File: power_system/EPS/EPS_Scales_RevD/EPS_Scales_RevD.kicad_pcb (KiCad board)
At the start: 4 copper layers, 95.2 x 66 mm, 253 parts, among them J1 Input Power, J10 DF11-16DP-2DSA, J11 DN-T1-GE3_VIS, J12 DF11-16DP-2DSA, J15 DN-T1-GE3_VIS, J16 Conn_01x04, J18 Conn_01x04, J2 Conn_01x01_Socket, J3 Conn_01x01_Socket, J4 Conn_01x01_Socket, J5 Conn_01x01_Socket, J6 DF11-16DP-2DSA, J7 DN-T1-GE3_VIS, J8 Conn_01x04, U1 LTC4365, U10 LTC4365, U11 LT8638S, U12 INA230, U13 TLV1704, U14 TLV1704, U2 LT8638SEVPBF, U3 INA230, U4 TLV1704, U5 LTC4365, U6 LT8638S, U7 LTC6902, U8 INA230, U9 TCA4307DGKR

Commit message: Lots of Goodies
Updated Con. Ops
Updated Footprint Assignments for R and C, WIP
Fixed Incorrect Resistor Values
Updated footprints for LEDs
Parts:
- removed C1, C14, C15, C17, C18, C19, C2, C20, C21, C22, C25, C3, C34, C35, C45, C5, C53, C54, C56, C57, C58, C59, C60, C61, C62, C63, C64, C65, C66, C67: 10u, Capacitor_SMD:C_1210_3225Metric
- removed C10, C29, C30, C37, C49: 0.1u, Capacitor_SMD:C_1210_3225Metric
- removed C12, C13, C32, C33, C51, C52: 47u, Capacitor_SMD:C_1210_3225Metric
- removed C16, C28, C36, C47, C55, C8: 1u, Capacitor_SMD:C_1210_3225Metric
- removed C23, C4, C43: 22u, Capacitor_SMD:C_1210_3225Metric
- removed C24, C44, C6: 1u, Capacitor_SMD:C_0603_1608Metric
- removed C26: 10n, Capacitor_SMD:C_0603_1608Metric
- removed C27, C9: 220p, Capacitor_SMD:C_0603_1608Metric
- removed C31, C38, C39: 22p, easyeda2kicad:C1206
- removed C46: 20n, Capacitor_SMD:C_0603_1608Metric
- removed C48: 1n, Capacitor_SMD:C_0603_1608Metric
- removed C7: 100n, Capacitor_SMD:C_0603_1608Metric
- removed D1, D10, D12, D3, D7, D9: 1N4151WS, RevC Footprints:SODFL2512X100N
- removed D11, D2, D8: GREEN, LED_SMD:LED_0603_1608Metric
- removed G*** (x3): LOGO, LOGO
- removed J1: Input Power, Connector_AMASS:AMASS_XT60PW-F_1x02_P7.20mm_Horizontal
- removed J10, J12, J6: DF11-16DP-2DSA, RevC Footprints:DF1116DP2DSA08
- removed J11, J15, J7: DN-T1-GE3_VIS, RevC Footprints:SISB46DN-T1-GE3
- removed J16, J18, J8: Conn_01x04, Connector_PinSocket_2.54mm:PinSocket_1x04_P2.54mm_Vertical
- removed J2, J3, J4, J5: Conn_01x01_Socket, MountingHole:MountingHole_2.5mm_Pad
- removed JP1, JP4, JP5: SolderJumper_2_Open, Jumper:SolderJumper-2_P1.3mm_Open_RoundedPad1.0x1.5mm
- removed L3: 10u, easyeda2kicad:IND-SMD_L13.8-W12.6_MHCC12050
- removed L4: 2.2u, RevC Footprints:XEL6030
- removed L5: 3.3u, RevC Footprints:XEL6030
- removed OV_TP1, OV_TP2, OV_TP3, TP1, TP10, TP11, TP12, TP13, TP14, TP15, TP16, TP17, TP18, TP19, TP2, TP20, TP28, TP29, TP3, TP30, TP31, TP32, TP33, TP34, TP35, TP36, TP37, TP38, TP39, TP4, TP40, TP41, TP42, TP43, TP44, TP45, TP46, TP47, TP48, TP49, TP5, TP50, TP51, TP52, TP53, TP6, TP7, TP8, TP9, UV_TP1, UV_TP2, UV_TP3: TestPoint, TestPoint:TestPoint_Pad_1.0x1.0mm
- removed R1, R28, R57: 12.9M, Resistor_SMD:R_0603_1608Metric
- removed R10, R38, R66: 10m, Resistor_SMD:R_2512_6332Metric
- removed R100, R101, R21, R23, R24, R25, R27, R31, R39, R5, R61, R77, R79, R8, R80, R81, R83, R94, R96, R97, R98: 100k, Resistor_SMD:R_0603_1608Metric
- removed R11, R67, R84: 10 (1206), Resistor_SMD:R_1206_3216Metric
- removed R12, R13, R14, R18, R19, R32, R42, R43, R44, R45, R46, R47, R48, R6, R62, R68, R69, R70, R74, R75, R85, R86, R87, R91, R92: 10k, Resistor_SMD:R_0603_1608Metric
- removed R15, R16, R17, R65, R71, R72, R73, R88, R89, R9, R90: 3.0k, Resistor_SMD:R_0603_1608Metric
- removed R2, R29, R58: 110k, Resistor_SMD:R_0603_1608Metric
- removed R20, R22, R4, R60, R76, R78, R93, R95: 1k, Resistor_SMD:R_0603_1608Metric
- removed R26, R82, R99: 4.7M, Resistor_SMD:R_0603_1608Metric
- removed R3, R30, R59: 190k, Resistor_SMD:R_0603_1608Metric
- removed R33, R63, R7: 105k, Resistor_SMD:R_0603_1608Metric
- removed R34: 14k, Resistor_SMD:R_0603_1608Metric
- removed R35: 17k, Resistor_SMD:R_0603_1608Metric
- removed R36: 25k, Resistor_SMD:R_0603_1608Metric
- removed R37: 5.5k, Resistor_SMD:R_0603_1608Metric
- removed R40: 150k, Resistor_SMD:R_0603_1608Metric
- removed R41: 50k, Resistor_SMD:R_0603_1608Metric
- removed R64: 22k, Resistor_SMD:R_0603_1608Metric
- removed U1, U10, U5: LTC4365, RevC Footprints:LTC4365
- removed U11, U6: LT8638S, RevC Footprints:LT8638SEVPBF
- removed U12, U3, U8: INA230, RevC Footprints:INA230AIRGTT
- removed U13, U14, U4: TLV1704, Package_SO:TSSOP-14_4.4x5mm_P0.65mm
- removed U2: LT8638SEVPBF, RevC Footprints:LT8638SEVPBF
- removed U7: LTC6902, RevC Footprints:LTC6902
- removed U9: TCA4307DGKR, easyeda2kicad:VSSOP-8_L3.0-W3.0-P0.65-LS4.9-BL
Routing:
- net +3.3V_OBC: track 235.8 -> 0.00 mm, vias 14 -> 0
- net GND: track 167.5 -> 0.00 mm, vias 93 -> 0
- net +V_Batt: track 143.8 -> 0.00 mm, vias 6 -> 0
- net SDA: track 120.9 -> 0.00 mm, vias 6 -> 0
- net SCL: track 119.0 -> 0.00 mm, vias 4 -> 0
- net SYNC_PHASE3: track 86.5 -> 0.00 mm, vias 3 -> 0
- net +5V_Perif: track 84.2 -> 0.00 mm, vias 5 -> 0
- net Net-(U2-BIAS): track 70.0 -> 0.00 mm, vias 2 -> 0
- net Net-(U11-BIAS): track 67.7 -> 0.00 mm, vias 8 -> 0
- net SYNC_PHASE1: track 66.8 -> 0.00 mm, vias 3 -> 0
- net ~{OBC_Toggle_Perif}: track 59.0 -> 0.00 mm, vias 1 -> 0
- net Net-(U6-BIAS): track 58.7 -> 0.00 mm
- net ~{WD_TOGGLE_OBC}: track 57.7 -> 0.00 mm, vias 5 -> 0
- net WDT_WDI_OBC: track 56.6 -> 0.00 mm, vias 1 -> 0
- net +20V_Jetson: track 56.0 -> 0.00 mm, vias 4 -> 0
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- removed copper zone on In2.Cu, net +V_Batt
- removed copper zone on In1.Cu, net GND
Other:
- board outline removed
- board text removed: "Designed by Luca Lanzillotta"
- board text removed: "SCALES EPS Viking 1-A"
- board text removed: "this should work..."

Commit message: More Goodies
Updated Inductor footprints with most readily available LCSC counterparts
Updated XT-60 connector
Updated Edge-Cuts board size
Updated Diode Footprints to fix DRC errors
Started Board layout and copper fills for power and ground
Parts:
- added C1: 10u, Capacitor_SMD:C_1210_3225Metric, F.Cu at (236.0, 106.9)
- added C10: 10n, EPS:C0402, F.Cu at (20.0, 50.5)
- added C11: 100n, EPS:C0402, F.Cu at (20.0, 52.6)
- added C13: 100n, EPS:C0402, F.Cu at (20.0, 54.8)
- added C14: 10p, EPS:C0402, F.Cu at (20.0, 56.9)
- added C15: 100n, EPS:C0402, F.Cu at (20.0, 59.1)
- added C16: 100n, EPS:C0402, F.Cu at (20.0, 61.2)
- added C17: 10u, Capacitor_SMD:C_1210_3225Metric, F.Cu at (32.7, 162.4)
- added C18: 10u, Capacitor_SMD:C_1210_3225Metric, F.Cu at (101.3, 147.0)
- added C19: 10u, Capacitor_SMD:C_1210_3225Metric, F.Cu at (101.3, 151.3)
- added C2: 10u, Capacitor_SMD:C_1210_3225Metric, F.Cu at (236.0, 102.7)
- added C20: 10u, Capacitor_SMD:C_1210_3225Metric, F.Cu at (101.3, 155.5)
- added C21: 10u, Capacitor_SMD:C_1210_3225Metric, F.Cu at (101.3, 159.8)
- added C22: 10u, Capacitor_SMD:C_1210_3225Metric, F.Cu at (101.3, 164.0)
- added C23: 22n, EPS:C0402, F.Cu at (79.7, 54.4)
- added C24: 220n, EPS:C0402, F.Cu at (79.7, 56.5)
- added C25: 2.2n, EPS:C0402, F.Cu at (79.7, 58.6)
- added C26: 10p, EPS:C0402, F.Cu at (79.7, 60.8)
- added C27: 100n, EPS:C0402, F.Cu at (79.7, 63.0)
- added C28: 100n, EPS:C0402, F.Cu at (79.7, 65.1)
- added C29: 0.1u, Capacitor_SMD:C_1210_3225Metric, F.Cu at (71.0, 57.7)
- added C3: 10u, Capacitor_SMD:C_1210_3225Metric, F.Cu at (236.0, 98.4)
- added C30: 47u, EPS:CASE-D_7343, F.Cu at (86.3, 56.3)
- added C31: 100n, EPS:C0402, F.Cu at (79.7, 67.2)
- added C32: 100n, EPS:C0402, F.Cu at (79.7, 69.4)
- added C33: 10u, Capacitor_SMD:C_1210_3225Metric, F.Cu at (32.7, 166.6)
- added C34: 220u, EPS:CASE-D_7343, F.Cu at (40.4, 156.5)
- added C35: 220u, EPS:CASE-D_7343, F.Cu at (40.4, 162.5)
- added C36: 22n, EPS:C0402, F.Cu at (103.7, 43.6)
- added C37: 0.1u, Capacitor_SMD:C_1210_3225Metric, F.Cu at (71.0, 61.9)
- added C38: 220n, EPS:C0402, F.Cu at (103.7, 45.8)
- added C39: 2.2n, EPS:C0402, F.Cu at (103.7, 47.9)
- added C4: 22n, EPS:C0402, F.Cu at (20.0, 46.2)
- added C40: 100n, EPS:C0402, F.Cu at (103.7, 50.0)
- added C41: 100n, EPS:C0402, F.Cu at (103.7, 52.2)
- added C42: 220u, EPS:CASE-D_7343, F.Cu at (76.1, 149.3)
- added C43: 220u, EPS:CASE-D_7343, F.Cu at (76.1, 155.3)
- added C44: 220u, EPS:CASE-D_7343, F.Cu at (76.1, 161.3)
- added C45: 220u, EPS:CASE-D_7343, F.Cu at (109.0, 147.9)
- added C46: 220u, EPS:CASE-D_7343, F.Cu at (109.0, 153.9)
- added C47: 220u, EPS:CASE-D_7343, F.Cu at (109.0, 159.9)
- added C48: 47u, EPS:CAP-SMD_L7.3-W4.3-FD, F.Cu at (127.0, 54.5)
- added C49: 10p, EPS:C0402, F.Cu at (103.7, 54.4)
- added C5: 220n, EPS:C0402, F.Cu at (20.0, 48.3)
- added C50: 100n, EPS:C0402, F.Cu at (103.7, 56.5)
- added C51: 100n, EPS:C0402, F.Cu at (103.7, 58.6)
- added C52: 47u, EPS:CAP-SMD_L7.3-W4.3-FD, F.Cu at (85.1, 38.9)
- added C53: 47u, EPS:CAP-SMD_L7.3-W4.3-FD, F.Cu at (127.0, 60.1)
- added C54: 47u, EPS:CAP-SMD_L7.3-W4.3-FD, F.Cu at (45.0, 59.2)
- added C55: 47u, EPS:CAP-SMD_L7.3-W4.3-FD, F.Cu at (45.0, 64.8)
- added C6: 220u, EPS:CASE-D_7343, F.Cu at (40.4, 150.5)
- added C63: 10u, Capacitor_SMD:C_1210_3225Metric, F.Cu at (68.4, 148.5)
- added C64: 10u, Capacitor_SMD:C_1210_3225Metric, F.Cu at (68.4, 152.7)
- added C65: 10u, Capacitor_SMD:C_1210_3225Metric, F.Cu at (68.4, 157.0)
- added C66: 10u, Capacitor_SMD:C_1210_3225Metric, F.Cu at (68.4, 161.2)
- added C67: 10u, Capacitor_SMD:C_1210_3225Metric, F.Cu at (68.4, 165.5)
- added C7: 10u, Capacitor_SMD:C_1210_3225Metric, F.Cu at (32.7, 149.6)
- added C8: 10u, Capacitor_SMD:C_1210_3225Metric, F.Cu at (32.7, 153.9)
- added C9: 10u, Capacitor_SMD:C_1210_3225Metric, F.Cu at (32.7, 158.1)
- added CN1: DF11-16DP-2DSA(08), EPS:CONN-TH_DF11-16DP-2DSA-08, F.Cu at (112.5, 38.5)
- added D1: 1N4151WS, EPS:SODFL2512X100N, F.Cu at (101.3, 167.6)
- added D10: 1N4151WS, EPS:SODFL2512X100N, F.Cu at (68.4, 169.1)
- added D11: GREEN, LED_SMD:LED_0603_1608Metric, F.Cu at (92.0, 169.3)
- added D12: 1N4151WS, EPS:SODFL2512X100N, F.Cu at (68.4, 172.0)
- added D14: BAS21,215, EPS:SOT-23-3_L2.9-W1.6-P1.90-LS2.8-BR, F.Cu at (91.1, 68.2)
- added D15: BAS21,215, EPS:SOT-23-3_L2.9-W1.6-P1.90-LS2.8-BR, F.Cu at (131.6, 65.0)
- added D16: BAS21,215, EPS:SOT-23-3_L2.9-W1.6-P1.90-LS2.8-BR, F.Cu at (49.0, 39.2)
- added D17: LED, EPS:LED0603-RD_RED, F.Cu at (92.2, 37.4)
- added D2: GREEN, LED_SMD:LED_0603_1608Metric, F.Cu at (124.9, 167.8)
- added D3: 1N4151WS, EPS:SODFL2512X100N, F.Cu at (101.3, 170.6)
- added D4: LED, EPS:LED0603-RD_RED, F.Cu at (48.8, 42.6)
- added D6: 1N4151WS, EPS:SODFL2512X100N, F.Cu at (32.7, 170.2)
- added D7: GREEN, LED_SMD:LED_0603_1608Metric, F.Cu at (56.3, 170.4)
- added D8: 1N4151WS, EPS:SODFL2512X100N, F.Cu at (32.7, 173.1)
- added D9: LED, EPS:LED0603-RD_RED, F.Cu at (116.6, 65.8)
- added J1: Input Power, Connector_AMASS:AMASS_XT60-M_1x02_P7.20mm_Vertical, F.Cu at (243.0, 98.4)
- added J10: DF11-16DP-2DSA, EPS:CONN-TH_DF11-16DP-2DSA-08, F.Cu at (69.6, 40.1)
- added J18: Conn_01x04, Connector_PinSocket_2.54mm:PinSocket_1x04_P2.54mm_Vertical, F.Cu at (83.3, 163.7)
- added J2: Conn_01x01_Socket, MountingHole:MountingHole_2.5mm_Pad, F.Cu at (160.0, 117.0)
- added J3: Conn_01x01_Socket, MountingHole:MountingHole_2.5mm_Pad, F.Cu at (160.0, 37.0)
- added J4: Conn_01x01_Socket, MountingHole:MountingHole_2.5mm_Pad, F.Cu at (239.0, 117.0)
- added J5: Conn_01x01_Socket, MountingHole:MountingHole_2.5mm_Pad, F.Cu at (240.0, 37.0)
- added J6: DF11-16DP-2DSA, EPS:CONN-TH_DF11-16DP-2DSA-08, F.Cu at (28.8, 41.1)
- added J7: Conn_01x04, Connector_PinSocket_2.54mm:PinSocket_1x04_P2.54mm_Vertical, F.Cu at (47.6, 164.9)
- added J8: Conn_01x04, Connector_PinSocket_2.54mm:PinSocket_1x04_P2.54mm_Vertical, F.Cu at (116.3, 162.3)
- added JP1: SolderJumper_2_Open, Jumper:SolderJumper-2_P1.3mm_Open_RoundedPad1.0x1.5mm, F.Cu at (120.7, 168.3)
- added JP2: SolderJumper_2_Open, Jumper:SolderJumper-2_P1.3mm_Open_RoundedPad1.0x1.5mm, F.Cu at (52.1, 170.9)
- added JP5: SolderJumper_2_Open, Jumper:SolderJumper-2_P1.3mm_Open_RoundedPad1.0x1.5mm, F.Cu at (87.8, 169.8)
- added L1: 4.7u, EPS:IND-SMD_L11.0-W10.0, F.Cu at (38.1, 50.7)
- added L2: 8.2u, EPS:IND-SMD_L11.5-W10.0, F.Cu at (66.5, 49.8)
- added L3: 12u, EPS:IND-SMD_L13.5-W12.6, F.Cu at (113.7, 49.5)
- added R1: 15k, EPS:R0402, F.Cu at (124.4, 170.2)
- added R10: 4.7k, EPS:R0402, F.Cu at (32.4, 68.2)
- added R100: 100k, Resistor_SMD:R_0603_1608Metric, F.Cu at (91.0, 155.1)
- added R101: 2k, EPS:R0402, F.Cu at (110.0, 68.2)
- added R102: 110k, EPS:R0402, F.Cu at (113.0, 57.5)
- added R103: 20.8k, EPS:R0402, F.Cu at (113.0, 59.6)
- added R104: 5k, EPS:R0402, F.Cu at (113.0, 61.8)
- added R107: 56.2k, EPS:R0402, F.Cu at (66.6, 60.9)
- added R108: 10k, EPS:R0402, F.Cu at (66.6, 63.1)
- added R11: 10 (1206), Resistor_SMD:R_1206_3216Metric, F.Cu at (107.0, 170.7)
- added R12: 10k, Resistor_SMD:R_0603_1608Metric, F.Cu at (116.0, 146.2)
- added R13: 10k, Resistor_SMD:R_0603_1608Metric, F.Cu at (116.0, 148.7)
- added R14: 10k, Resistor_SMD:R_0603_1608Metric, F.Cu at (116.0, 151.2)
- added R15: 3.0k, Resistor_SMD:R_0603_1608Metric, F.Cu at (116.0, 153.7)
- added R16: 3.0k, Resistor_SMD:R_0603_1608Metric, F.Cu at (116.0, 156.2)
- added R17: 3.0k, Resistor_SMD:R_0603_1608Metric, F.Cu at (116.0, 158.7)
- added R18: 10k, Resistor_SMD:R_0603_1608Metric, F.Cu at (120.0, 146.2)
- added R19: 10k, Resistor_SMD:R_0603_1608Metric, F.Cu at (120.0, 148.7)
- added R2: 10 (1206), Resistor_SMD:R_1206_3216Metric, F.Cu at (38.3, 173.2)
- added R20: 1k, Resistor_SMD:R_0603_1608Metric, F.Cu at (120.0, 151.2)
- added R21: 100k, Resistor_SMD:R_0603_1608Metric, F.Cu at (120.0, 153.7)
- added R22: 1k, Resistor_SMD:R_0603_1608Metric, F.Cu at (120.0, 156.2)
- added R23: 100k, Resistor_SMD:R_0603_1608Metric, F.Cu at (120.0, 158.7)
- added R24: 100k, Resistor_SMD:R_0603_1608Metric, F.Cu at (124.0, 146.2)
- added R25: 100k, Resistor_SMD:R_0603_1608Metric, F.Cu at (124.0, 148.7)
- added R26: 4.7M, Resistor_SMD:R_0603_1608Metric, F.Cu at (124.0, 151.2)
- added R27: 100k, Resistor_SMD:R_0603_1608Metric, F.Cu at (124.0, 153.7)
- added R28: 1k, EPS:R0402, F.Cu at (35.4, 57.4)
- added R29: 10k, Resistor_SMD:R_0603_1608Metric, F.Cu at (47.3, 153.8)
- added R3: 15k, EPS:R0402, F.Cu at (32.4, 57.4)
- added R30: 3.0k, Resistor_SMD:R_0603_1608Metric, F.Cu at (47.3, 156.3)
- added R31: 3.0k, Resistor_SMD:R_0603_1608Metric, F.Cu at (47.3, 158.8)
- added R32: 3.0k, Resistor_SMD:R_0603_1608Metric, F.Cu at (47.3, 161.3)
- added R33: 10k, Resistor_SMD:R_0603_1608Metric, F.Cu at (51.3, 148.7)
- added R34: 14k, Resistor_SMD:R_0603_1608Metric, F.Cu at (75.9, 45.4)
- added R35: 17k, Resistor_SMD:R_0603_1608Metric, F.Cu at (75.9, 47.9)
- added R36: 5.1k, EPS:R0402, F.Cu at (35.4, 59.6)
- added R37: 1k, EPS:R0402, F.Cu at (35.4, 61.7)
- added R38: 10k, Resistor_SMD:R_0603_1608Metric, F.Cu at (51.3, 151.3)
- added R39: 1k, Resistor_SMD:R_0603_1608Metric, F.Cu at (51.3, 153.8)
- added R4: 15k, EPS:R0402, F.Cu at (32.4, 59.6)
- added R40: 4.7k, EPS:R0402, F.Cu at (60.6, 56.6)
- added R41: 15k, EPS:R0402, F.Cu at (60.6, 58.8)
- added R42: 10k, Resistor_SMD:R_0603_1608Metric, F.Cu at (75.9, 50.4)
- added R43: 10k, Resistor_SMD:R_0603_1608Metric, F.Cu at (75.9, 52.9)
- added R44: 10k, Resistor_SMD:R_0603_1608Metric, F.Cu at (75.9, 55.4)
- added R45: 10k, Resistor_SMD:R_0603_1608Metric, F.Cu at (75.9, 57.9)
- added R46: 10k, Resistor_SMD:R_0603_1608Metric, F.Cu at (75.9, 60.4)
- added R47: 10k, Resistor_SMD:R_0603_1608Metric, F.Cu at (75.9, 63.0)
- added R48: 10k, Resistor_SMD:R_0603_1608Metric, F.Cu at (75.9, 65.5)
- added R49: 100k, Resistor_SMD:R_0603_1608Metric, F.Cu at (51.3, 156.3)
- added R5: 220, EPS:R0402, F.Cu at (32.4, 61.7)
- added R50: 15k, EPS:R0402, F.Cu at (35.4, 63.9)
- added R51: 1k, Resistor_SMD:R_0603_1608Metric, F.Cu at (51.3, 158.8)
- added R52: 110k, EPS:R0402, F.Cu at (35.4, 66.0)
- added R53: 47k, EPS:R0402, F.Cu at (35.4, 68.2)
- added R54: 2k, EPS:R0402, F.Cu at (38.5, 57.4)
- added R55: 196k, EPS:R0402, F.Cu at (38.5, 59.6)
- added R56: 10k, EPS:R0402, F.Cu at (38.5, 61.7)
- added R57: 1k, EPS:R0402, F.Cu at (60.6, 60.9)
- added R58: 220, EPS:R0402, F.Cu at (60.6, 63.1)
- added R59: 15k, EPS:R0402, F.Cu at (60.6, 65.2)
- added R6: 15k, EPS:R0402, F.Cu at (32.4, 63.9)
- added R60: 15k, EPS:R0402, F.Cu at (63.6, 56.6)
- added R61: 15k, EPS:R0402, F.Cu at (63.6, 58.8)
- added R62: 110k, EPS:R0402, F.Cu at (63.6, 60.9)
- added R63: 47k, EPS:R0402, F.Cu at (63.6, 63.1)
- added R64: 2k, EPS:R0402, F.Cu at (63.6, 65.2)
- added R65: 240k, EPS:R0402, F.Cu at (66.6, 56.6)
- added R66: 10k, EPS:R0402, F.Cu at (66.6, 58.8)
- added R67: 100k, Resistor_SMD:R_0603_1608Metric, F.Cu at (51.3, 161.3)
- added R68: 100k, Resistor_SMD:R_0603_1608Metric, F.Cu at (55.4, 148.7)
- added R69: 100k, Resistor_SMD:R_0603_1608Metric, F.Cu at (55.4, 151.3)
- added R7: 15k, EPS:R0402, F.Cu at (32.4, 66.0)
- added R70: 4.7M, Resistor_SMD:R_0603_1608Metric, F.Cu at (55.4, 153.8)
- added R71: 100k, Resistor_SMD:R_0603_1608Metric, F.Cu at (55.4, 156.3)
- added R72: 15k, EPS:R0402, F.Cu at (55.8, 172.8)
- added R73: 1k, EPS:R0402, F.Cu at (107.0, 57.5)
- added R74: 2k, EPS:R0402, F.Cu at (107.0, 59.6)
- added R75: 1k, EPS:R0402, F.Cu at (107.0, 61.8)
- added R76: 15k, EPS:R0402, F.Cu at (107.0, 63.9)
- added R77: 220, EPS:R0402, F.Cu at (107.0, 66.0)
- added R78: 4.7k, EPS:R0402, F.Cu at (107.0, 68.2)
- added R79: 15k, EPS:R0402, F.Cu at (110.0, 57.5)
- added R8: 10k, Resistor_SMD:R_0603_1608Metric, F.Cu at (47.3, 148.7)
- added R80: 15k, EPS:R0402, F.Cu at (110.0, 59.6)
- added R81: 15k, EPS:R0402, F.Cu at (110.0, 61.8)
- added R82: 15k, EPS:R0402, F.Cu at (110.0, 63.9)
- added R83: 47k, EPS:R0402, F.Cu at (110.0, 66.0)
- added R84: 10 (1206), Resistor_SMD:R_1206_3216Metric, F.Cu at (74.0, 172.1)
- added R85: 10k, Resistor_SMD:R_0603_1608Metric, F.Cu at (83.0, 147.6)
- added R86: 10k, Resistor_SMD:R_0603_1608Metric, F.Cu at (83.0, 150.1)
- added R87: 10k, Resistor_SMD:R_0603_1608Metric, F.Cu at (83.0, 152.6)
- added R88: 3.0k, Resistor_SMD:R_0603_1608Metric, F.Cu at (83.0, 155.1)
- added R89: 3.0k, Resistor_SMD:R_0603_1608Metric, F.Cu at (83.0, 157.6)
- added R9: 10k, Resistor_SMD:R_0603_1608Metric, F.Cu at (47.3, 151.3)
- added R90: 3.0k, Resistor_SMD:R_0603_1608Metric, F.Cu at (83.0, 160.2)
- added R91: 10k, Resistor_SMD:R_0603_1608Metric, F.Cu at (87.0, 147.6)
- added R92: 10k, Resistor_SMD:R_0603_1608Metric, F.Cu at (87.0, 150.1)
- added R93: 1k, Resistor_SMD:R_0603_1608Metric, F.Cu at (87.0, 152.6)
- added R94: 100k, Resistor_SMD:R_0603_1608Metric, F.Cu at (87.0, 155.1)
- added R95: 1k, Resistor_SMD:R_0603_1608Metric, F.Cu at (87.0, 157.6)
- added R96: 100k, Resistor_SMD:R_0603_1608Metric, F.Cu at (87.0, 160.2)
- added R97: 100k, Resistor_SMD:R_0603_1608Metric, F.Cu at (91.0, 147.6)
- added R98: 100k, Resistor_SMD:R_0603_1608Metric, F.Cu at (91.0, 150.1)
- added R99: 4.7M, Resistor_SMD:R_0603_1608Metric, F.Cu at (91.0, 152.6)
- added TP1: TestPoint, TestPoint:TestPoint_Pad_1.0x1.0mm, F.Cu at (23.3, 46.6)
- added TP10: TestPoint, TestPoint:TestPoint_Pad_1.0x1.0mm, F.Cu at (105.7, 164.4)
- added TP11: TestPoint, TestPoint:TestPoint_Pad_1.0x1.0mm, F.Cu at (105.7, 167.5)
- added TP12: TestPoint, TestPoint:TestPoint_Pad_1.0x1.0mm, F.Cu at (108.7, 164.4)
- added TP13: TestPoint, TestPoint:TestPoint_Pad_1.0x1.0mm, F.Cu at (108.7, 167.5)
- added TP14: TestPoint, TestPoint:TestPoint_Pad_1.0x1.0mm, F.Cu at (111.8, 164.4)
- added TP15: TestPoint, TestPoint:TestPoint_Pad_1.0x1.0mm, F.Cu at (43.1, 170.1)
- added TP16: TestPoint, TestPoint:TestPoint_Pad_1.0x1.0mm, F.Cu at (123.5, 44.0)
- added TP17: TestPoint, TestPoint:TestPoint_Pad_1.0x1.0mm, F.Cu at (123.5, 47.1)
- added TP18: TestPoint, TestPoint:TestPoint_Pad_1.0x1.0mm, F.Cu at (123.5, 50.1)
- added TP19: TestPoint, TestPoint:TestPoint_Pad_1.0x1.0mm, F.Cu at (126.5, 44.0)
- added TP2: TestPoint, TestPoint:TestPoint_Pad_1.0x1.0mm, F.Cu at (23.3, 49.7)
- added TP20: TestPoint, TestPoint:TestPoint_Pad_1.0x1.0mm, F.Cu at (126.5, 47.1)
- added TP21: TestPoint, TestPoint:TestPoint_Pad_1.0x1.0mm, F.Cu at (126.5, 50.1)
- added TP22: TestPoint, TestPoint:TestPoint_Pad_1.0x1.0mm, F.Cu at (79.4, 45.6)
- added TP23: TestPoint, TestPoint:TestPoint_Pad_1.0x1.0mm, F.Cu at (79.4, 48.7)
- added TP24: TestPoint, TestPoint:TestPoint_Pad_1.0x1.0mm, F.Cu at (79.4, 51.8)
- added TP25: TestPoint, TestPoint:TestPoint_Pad_1.0x1.0mm, F.Cu at (23.3, 58.8)
- added TP26: TestPoint, TestPoint:TestPoint_Pad_1.0x1.0mm, F.Cu at (26.3, 46.6)
- added TP27: TestPoint, TestPoint:TestPoint_Pad_1.0x1.0mm, F.Cu at (26.3, 49.7)
- added TP28: TestPoint, TestPoint:TestPoint_Pad_1.0x1.0mm, F.Cu at (26.3, 52.7)
- added TP29: TestPoint, TestPoint:TestPoint_Pad_1.0x1.0mm, F.Cu at (26.3, 55.8)
- added TP3: TestPoint, TestPoint:TestPoint_Pad_1.0x1.0mm, F.Cu at (23.3, 52.7)
- added TP30: TestPoint, TestPoint:TestPoint_Pad_1.0x1.0mm, F.Cu at (26.3, 58.8)
- added TP31: TestPoint, TestPoint:TestPoint_Pad_1.0x1.0mm, F.Cu at (82.5, 45.6)
- added TP32: TestPoint, TestPoint:TestPoint_Pad_1.0x1.0mm, F.Cu at (82.5, 48.7)
- added TP33: TestPoint, TestPoint:TestPoint_Pad_1.0x1.0mm, F.Cu at (82.5, 51.8)
- added TP34: TestPoint, TestPoint:TestPoint_Pad_1.0x1.0mm, F.Cu at (85.5, 45.6)
- added TP35: TestPoint, TestPoint:TestPoint_Pad_1.0x1.0mm, F.Cu at (85.5, 48.7)
- added TP36: TestPoint, TestPoint:TestPoint_Pad_1.0x1.0mm, F.Cu at (85.5, 51.8)
- added TP37: TestPoint, TestPoint:TestPoint_Pad_1.0x1.0mm, F.Cu at (129.6, 44.0)
- added TP38: TestPoint, TestPoint:TestPoint_Pad_1.0x1.0mm, F.Cu at (29.4, 46.6)
- added TP39: TestPoint, TestPoint:TestPoint_Pad_1.0x1.0mm, F.Cu at (129.6, 47.1)
- added TP4: TestPoint, TestPoint:TestPoint_Pad_1.0x1.0mm, F.Cu at (23.3, 55.8)
- added TP40: TestPoint, TestPoint:TestPoint_Pad_1.0x1.0mm, F.Cu at (129.6, 50.1)
- added TP41: TestPoint, TestPoint:TestPoint_Pad_1.0x1.0mm, F.Cu at (132.6, 44.0)
- added TP42: TestPoint, TestPoint:TestPoint_Pad_1.0x1.0mm, F.Cu at (132.6, 47.1)
- added TP43: TestPoint, TestPoint:TestPoint_Pad_1.0x1.0mm, F.Cu at (132.6, 50.1)
- added TP44: TestPoint, TestPoint:TestPoint_Pad_1.0x1.0mm, F.Cu at (29.4, 49.7)
- added TP45: TestPoint, TestPoint:TestPoint_Pad_1.0x1.0mm, F.Cu at (29.4, 52.7)
- added TP46: TestPoint, TestPoint:TestPoint_Pad_1.0x1.0mm, F.Cu at (29.4, 55.8)
- added TP47: TestPoint, TestPoint:TestPoint_Pad_1.0x1.0mm, F.Cu at (111.8, 167.5)
- added TP48: TestPoint, TestPoint:TestPoint_Pad_1.0x1.0mm, F.Cu at (72.7, 165.9)
- added TP49: TestPoint, TestPoint:TestPoint_Pad_1.0x1.0mm, F.Cu at (72.7, 168.9)
- added TP5: TestPoint, TestPoint:TestPoint_Pad_1.0x1.0mm, F.Cu at (37.0, 167.0)
- added TP50: TestPoint, TestPoint:TestPoint_Pad_1.0x1.0mm, F.Cu at (75.8, 165.9)
- added TP51: TestPoint, TestPoint:TestPoint_Pad_1.0x1.0mm, F.Cu at (75.8, 168.9)
- added TP52: TestPoint, TestPoint:TestPoint_Pad_1.0x1.0mm, F.Cu at (78.8, 165.9)
- added TP53: TestPoint, TestPoint:TestPoint_Pad_1.0x1.0mm, F.Cu at (78.8, 168.9)
- added TP6: TestPoint, TestPoint:TestPoint_Pad_1.0x1.0mm, F.Cu at (37.0, 170.1)
- added TP7: TestPoint, TestPoint:TestPoint_Pad_1.0x1.0mm, F.Cu at (40.1, 167.0)
- added TP8: TestPoint, TestPoint:TestPoint_Pad_1.0x1.0mm, F.Cu at (40.1, 170.1)
- added TP9: TestPoint, TestPoint:TestPoint_Pad_1.0x1.0mm, F.Cu at (43.1, 167.0)
- added U1: LT8612EUDE#PBF, EPS:QFN-28_L6.0-W3.0-P0.50-BL-EP, F.Cu at (43.0, 39.2)
- added U12: TPS1HB08BQPWPRQ1, EPS:HTSSOP-16_L5.0-W4.4-P0.65-LS6.4-TL-EP2.9, F.Cu at (127.2, 38.2)
- added U13: LT8612EUDE#PBF, EPS:QFN-28_L6.0-W3.0-P0.50-BL-EP, F.Cu at (125.7, 65.1)
- added U14: TLV1704, Package_SO:TSSOP-14_4.4x5mm_P0.65mm, F.Cu at (90.0, 164.7)
- added U15: TPS1HB08BQPWPRQ1, EPS:HTSSOP-16_L5.0-W4.4-P0.65-LS6.4-TL-EP2.9, F.Cu at (26.0, 64.0)
- added U16: INA260AIPWR, EPS:TSSOP-16_L5.0-W4.4-P0.65-LS6.4-BL-1, F.Cu at (118.1, 60.4)
- added U17: TPS1HB08BQPWPRQ1, EPS:HTSSOP-16_L5.0-W4.4-P0.65-LS6.4-TL-EP2.9, F.Cu at (85.7, 63.0)
- added U2: INA260AIPWR, EPS:TSSOP-16_L5.0-W4.4-P0.65-LS6.4-BL-1, F.Cu at (48.9, 49.2)
- added U3: LT8612EUDE#PBF, EPS:QFN-28_L6.0-W3.0-P0.50-BL-EP, F.Cu at (85.1, 68.3)
- added U4: TLV1704, Package_SO:TSSOP-14_4.4x5mm_P0.65mm, F.Cu at (122.9, 163.3)
- added U5: INA260AIPWR, EPS:TSSOP-16_L5.0-W4.4-P0.65-LS6.4-BL-1, F.Cu at (90.7, 48.2)
- added U6: TLV1704, Package_SO:TSSOP-14_4.4x5mm_P0.65mm, F.Cu at (54.3, 165.8)
- added U7: LTC6902, EPS:MSOP-10_L3.0-W3.0-P0.50-LS5.0-BL, F.Cu at (92.3, 62.7)
- added U9: TCA4307DGKR, EPS:VSSOP-8_L3.0-W3.0-P0.65-LS4.9-BL, F.Cu at (70.5, 67.5)
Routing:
- added copper zone on In2.Cu, net +V_Batt
- added copper zone on In1.Cu, net GND
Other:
- board outline added: 100 x 100 mm

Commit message: Layout.....
Pain
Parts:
- moved TP3 107.7 mm to (-75.9, 10.7)
- moved J6 106.9 mm to (-74.9, 15.2)
- moved TP26 106.0 mm to (-79.1, 35.6)
- moved TP2 104.6 mm to (-73.8, 10.7)
- moved TP1 101.5 mm to (-71.6, 10.7)
- moved D16 98.9 mm to (-49.9, 37.4)
- moved C4 97.3 mm to (-76.7, 35.7)
- moved U15 87.3 mm to (-61.0, 56.0)
- moved C10 86.7 mm to (-65.8, 38.2)
- moved C13 86.7 mm to (-65.8, 42.5)
- moved C14 86.7 mm to (-65.8, 44.7)
- moved C15 86.7 mm to (-65.8, 46.9)
- moved C16 86.7 mm to (-65.8, 49.0)
- moved C5 86.7 mm to (-65.8, 36.1)
- moved D4 86.7 mm to (-37.0, 30.4)
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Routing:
- net +20V_Jetson: track 0.00 -> 6.00 mm
- net +V_Batt: track 0.00 -> 4.37 mm, vias 0 -> 3
- net GND: track 0.00 -> 4.13 mm, vias 0 -> 3
- net Net-(J6-Pad6): track 0.00 -> 3.70 mm
- net Net-(J6-Pad8): track 0.00 -> 3.63 mm
- net Net-(J6-Pad10): track 0.00 -> 3.59 mm
- net WDT_WDI_Jetson: track 0.00 -> 2.00 mm
- added copper zone on F.Cu, net GND

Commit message: MInor PCB Layout Updates
Started Routing the jetson subsystem
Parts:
- moved R40 84.7 mm to (57.6, 62.2)
- moved R41 84.7 mm to (57.6, 64.3)
- moved R57 84.7 mm to (57.6, 66.5)
- moved R58 84.7 mm to (57.6, 68.6)
- moved R59 84.7 mm to (57.6, 70.8)
- moved D4 58.1 mm to (-61.2, 83.2), turned to 180 degrees
- moved D16 37.5 mm to (-58.5, 74.0), turned to -90 degrees
- moved C16 36.0 mm to (-32.3, 35.7), turned to -90 degrees
- moved C15 35.2 mm to (-31.6, 38.5)
- moved R28 34.4 mm to (-61.7, 77.7)
- moved R5 33.1 mm to (-61.7, 81.6)
- moved R3 33.1 mm to (-51.0, 78.2)
- moved R4 32.2 mm to (-51.0, 79.5)
- moved R50 30.8 mm to (-61.7, 80.3)
- moved R6 28.6 mm to (-61.7, 79.0)
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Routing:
- net GND: track 4.13 -> 18.9 mm, vias 3 -> 15
- net Net-(U1-BIAS): track 0.00 -> 6.10 mm
- net Net-(U15-~{ST}): track 0.00 -> 3.85 mm
- net Net-(U15-GND): track 0.00 -> 3.45 mm
- net ~{WD_EN_JETSON}: track 0.00 -> 3.12 mm
- net Net-(U15-SEL1): track 0.00 -> 3.02 mm
- net Net-(U15-LATCH): track 0.00 -> 2.63 mm
- net Net-(U15-SEL2): track 0.00 -> 2.59 mm
- net +3.3V_OBC: track 0.00 -> 2.47 mm
- net Net-(U15-SNS): track 0.00 -> 2.35 mm
- net Net-(U15-DIA_EN): track 0.00 -> 2.22 mm
- added copper zone on In2.Cu, net +20V_Jetson
- added copper zone on F.Cu, net Net-(C4-Pad1)
- added copper zone on F.Cu, net Net-(U1-BIAS)
- added copper zone on F.Cu, net Net-(U15-GND)
- added copper zone on F.Cu, net Net-(U15-LATCH)
- added copper zone on F.Cu, net Net-(U15-SNS)
- added copper zone on F.Cu, net Net-(U15-~{ST})
- added copper zone on F.Cu, net ~{WD_EN_JETSON}

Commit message: Board Layout complete
Its a bit messy but I think ive managed to get the loop areas small enough, and the board to represent what is on the schematic. Probably would be a good idea to get a look at it from someone more reputable than myself on how this board should be layed out.
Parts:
- removed C30: 47u, EPS:CASE-D_7343
- added C56: 47u, EPS:CAP-SMD_L7.3-W4.3-FD, F.Cu at (180.9, 110.1)
- added G***: LOGO, LOGO, F.Cu at (195.2, 39.0)
- added G***: LOGO, LOGO, F.Cu at (175.1, 38.5)
- added R105: 15k, EPS:R0402, F.Cu at (167.6, 51.5)
- added TP54: TestPoint, TestPoint:TestPoint_Pad_1.0x1.0mm, F.Cu at (208.7, 91.6)
- moved TP3 321.3 mm to (225.9, 120.9), turned to 180 degrees
- moved TP2 317.3 mm to (223.8, 120.9), turned to 180 degrees
- moved J6 315.8 mm to (224.2, 116.7), turned to 180 degrees
- moved TP1 313.3 mm to (221.6, 120.9), turned to 180 degrees
- moved TP26 309.2 mm to (224.8, 92.7)
- moved C14 301.7 mm to (229.5, 106.4), turned to -90 degrees
- moved C4 300.9 mm to (218.3, 95.0), turned to -90 degrees
- moved TP4 300.7 mm to (228.0, 120.9), turned to 180 degrees
- moved TP28 298.1 mm to (231.2, 106.4), turned to 90 degrees
- moved TP46 296.9 mm to (230.2, 120.9), turned to 180 degrees
- moved C13 295.9 mm to (224.4, 100.1)
- moved TP30 295.5 mm to (232.3, 93.1)
- moved C10 291.8 mm to (220.5, 94.3), turned to 180 degrees
- moved C5 290.6 mm to (220.4, 86.7), turned to 180 degrees
- moved TP27 288.3 mm to (222.8, 95.9), turned to -90 degrees
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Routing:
- net GND: track 18.9 -> 154.1 mm, vias 15 -> 116
- net +3.3V_OBC: track 2.47 -> 113.1 mm, vias 0 -> 8
- net SDA: track 0.00 -> 84.2 mm, vias 0 -> 9
- net SCL: track 0.00 -> 79.4 mm, vias 0 -> 4
- net WDT_WDI_OBC: track 0.00 -> 65.8 mm, vias 0 -> 4
- net ~{WD_EN_OBC}: track 0.00 -> 63.8 mm, vias 0 -> 1
- net WDT_WDI_Jetson: track 2.00 -> 61.0 mm, vias 0 -> 2
- net SYNC_PHASE3: track 0.00 -> 58.5 mm, vias 0 -> 4
- net OBC_EN_JETSON: track 0.00 -> 58.2 mm
- net WDT_WDI_Perif: track 0.00 -> 57.0 mm, vias 0 -> 2
- net OBC SCL: track 0.00 -> 46.4 mm, vias 0 -> 1
- net OBC SDA: track 0.00 -> 45.8 mm, vias 0 -> 1
- net ~{WD_EN_PERIF}: track 0.00 -> 45.6 mm
- net Net-(D8-K): track 0.00 -> 38.3 mm, vias 0 -> 4
- net Net-(U6C--): track 0.00 -> 37.1 mm, vias 0 -> 4
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- added copper zone on F.Cu, net +20V_Jetson
- added copper zone on In2.Cu, net +3.3V_Jetson
- added copper zone on F.Cu, net +3.3V_OBC
- added copper zone on In2.Cu, net +3.3V_OBC
- added copper zone on F.Cu, net +5V_PERIF
- added copper zone on In2.Cu, net +5V_PERIF
- added copper zone on F.Cu, net +V_Batt
- added copper zone on F.Cu, net /Jetson_Subsystem/WD_Jetson/WDT-VIN
- added copper zone on F.Cu, net Net-(C11-Pad2)
- added copper zone on F.Cu, net Net-(C23-Pad1)
- added copper zone on F.Cu, net Net-(C27-Pad2)
- added copper zone on F.Cu, net Net-(C36-Pad1)
- added copper zone on F.Cu, net Net-(C40-Pad2)
- added copper zone on F.Cu, net Net-(U13-BIAS)
- added copper zone on F.Cu, net Net-(U3-BIAS)
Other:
- outline, holes or cut-outs redrawn

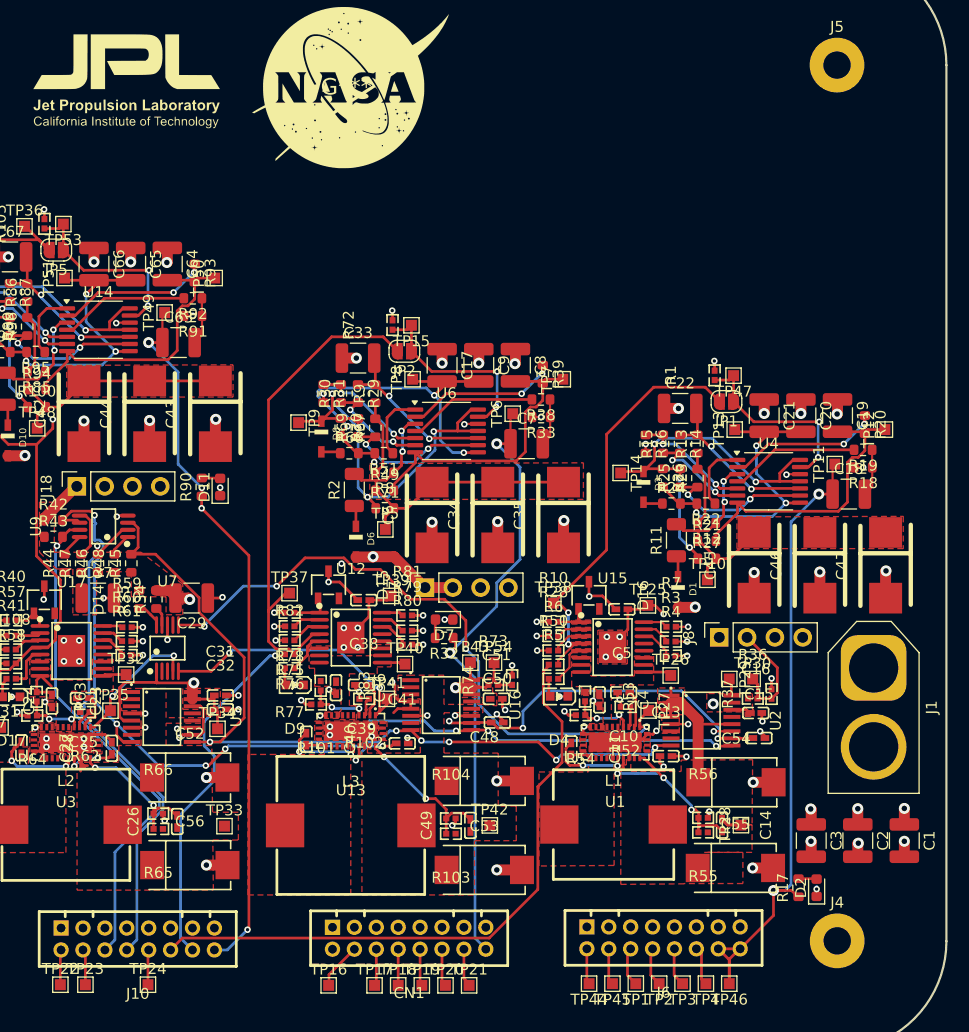
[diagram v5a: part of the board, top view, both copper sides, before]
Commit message: Updated with JLC requirements
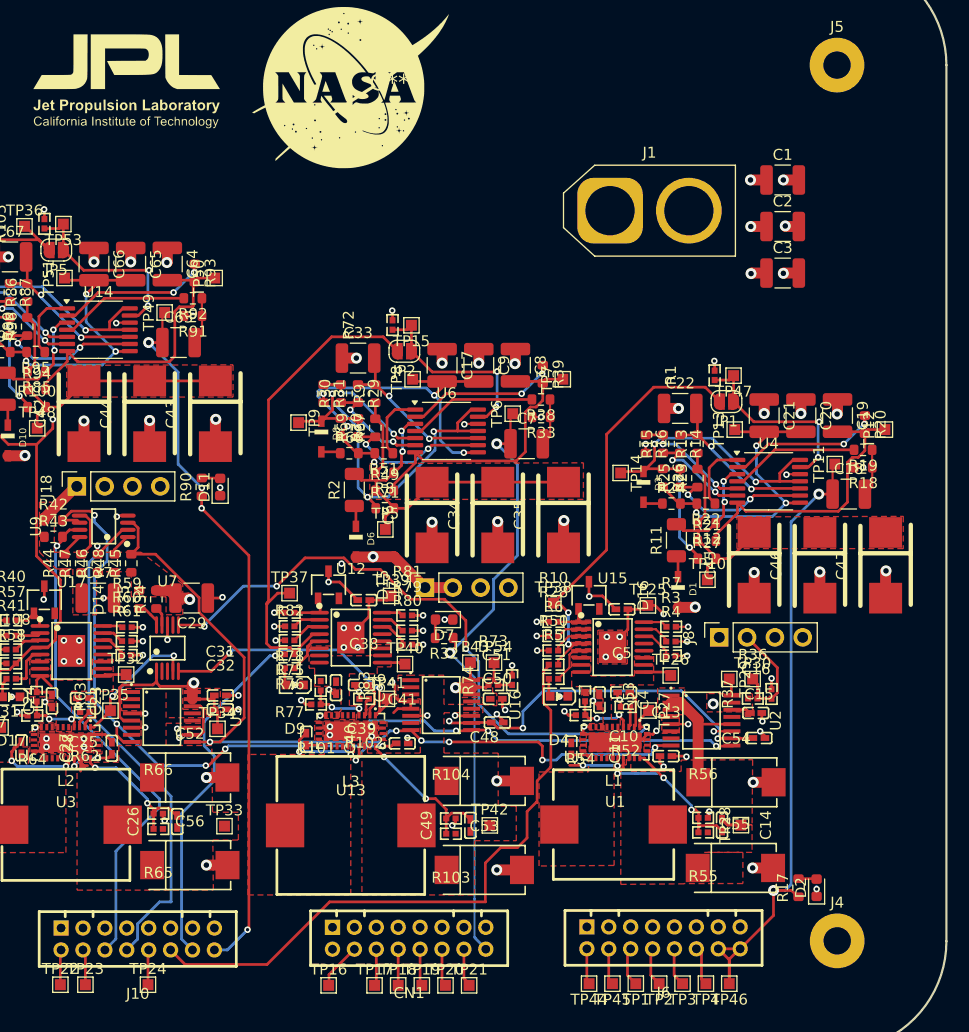
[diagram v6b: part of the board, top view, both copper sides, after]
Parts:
- moved C1 61.3 mm to (235.0, 47.5), turned to 0 degrees
- moved C2 56.5 mm to (235.0, 51.7), turned to 0 degrees
- moved C3 51.9 mm to (235.0, 56.0), turned to 0 degrees
- moved J1 48.2 mm to (219.3, 50.3), turned to 0 degrees
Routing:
- net Net-(U1-BIAS): track 17.9 -> 15.3 mm
- net Net-(U1-BST): track 7.46 -> 5.07 mm
- net OBC_EN_JETSON: track 58.2 -> 57.2 mm
- net Net-(U14B-+): track 26.7 -> 27.4 mm
- net OBC SCL: track 46.4 -> 47.0 mm
- net SDA: track 84.2 -> 84.8 mm
